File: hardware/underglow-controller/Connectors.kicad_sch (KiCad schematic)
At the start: 3 parts, among them J4 DTM1312PA12PBR008, J5 Conn_01x10

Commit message: i can't believe what they did to my boy
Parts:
- removed H1: MountingHole_Pad, MountingHole:MountingHole_3.2mm_M3_DIN965_Pad, symbol Mechanical:MountingHole_Pad
- added D5: D_Small, Diode_SMD:D_SOD-123F, symbol Device:D_Small
- added D7, D8: PESD2CANFD24V-T, Package_TO_SOT_SMD:SOT-23, symbol Device:D_TVS_Dual_AAC
- added F2: Fuse, ConeCodes:Keystone-3587-10TR, symbol Device:Fuse
- added J3: Conn_01x04, Connector_PinHeader_1.27mm:PinHeader_1x04_P1.27mm_Vertical, symbol Connector_Generic:Conn_01x04
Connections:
- net CAN_N: now also J4.B1, D8.2 (A2); no longer J4.B12
- net CAN_P: now also J4.B12, D8.1 (A1); no longer J4.B1
- net CONN_ESP_USB_D_N: now also J4.B4, D7.1 (A1); no longer J5.6 (Pin_6)
- net CONN_ESP_USB_D_P: now also J4.B5, D7.2 (A2); no longer J5.5 (Pin_5)
- net CONN_RP_USB_D_N: now also J3.3 (Pin_3); no longer J5.4 (Pin_4)
- net CONN_RP_USB_D_P: now also J3.2 (Pin_2); no longer J5.3 (Pin_3)
- net GND: now also D7.3 (common), D8.3 (common), J3.4 (Pin_4); no longer J4.A12
- net VBAT: now also D5.2 (A); no longer J4.A11
- net GPO4 renamed VOUT
- net GPO5: no longer names the net of J4.A6
- net GPO6: no longer names the net of J4.A5
- new net FUSE_IN: F2.2, J4.A12
- new net FUSE_OUT: F2.1
- new net VIN: D5.1 (K)
- no-connect marks 1 -> 2

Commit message: urmom
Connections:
- net VBAT is gone; now on net IGNITION: D5.2 (A)
- net CAN_N: now also J4.B12; no longer J4.B1
- net CAN_P: now also J4.B1; no longer J4.B12
- net GND: now also J4.A5
- net LEDA_OUT: now also J4.A4
- net VOUT: now also J4.A11; no longer J4.A4
- net IGNITION: now reaches J4.A6
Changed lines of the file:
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@@
+    (stroke (width 0) (type default) (color 0 0 0 0))
+  )
+  (wire (pts (xy 101.6 69.215) (xy 116.205 69.215))
     (stroke (width 0) (type default) (color 0 0 0 0))
   )
@@
     (stroke (width 0) (type default) (color 0 0 0 0))
   )
+  (wire (pts (xy 96.52 66.675) (xy 116.205 66.675))
+    (stroke (width 0) (type default) (color 0 0 0 0))
+  )
   (wire (pts (xy 57.785 84.455) (xy 70.485 84.455))
     (stroke (width 0) (type default) (color 0 0 0 0))
   )
-  (wire (pts (xy 101.6 64.135) (xy 116.205 64.135))
+  (wire (pts (xy 101.6 81.915) (xy 116.205 81.915))
     (stroke (width 0) (type default) (color 0 0 0 0))
   )
@@
     (stroke (width 0) (type default) (color 0 0 0 0))
   )
+  (wire (pts (xy 96.52 64.135) (xy 116.205 64.135))
+    (stroke (width 0) (type default) (color 0 0 0 0))
+  )
   (wire (pts (xy 96.52 79.375) (xy 116.205 79.375))
     (stroke (width 0) (type default) (color 0 0 0 0))
   )
   (wire (pts (xy 141.605 56.515) (xy 168.91 56.515))
-    (stroke (width 0) (type default) (color 0 0 0 0))
-  )
-  (wire (pts (xy 34.925 60.96) (xy 53.34 60.96))
-    (stroke (width 0) (type default) (color 0 0 0 0))
-  )
-  (wire (pts (xy 84.455 93.345) (xy 104.14 93.345))
     (stroke (width 0) (type default) (color 0 0 0 0))
   )
@@
     (effects (font (size 1.27 1.27)) (justify right bottom))
   )
-  (label "VBAT" (at 20.32 82.55 0)
+  (label "IGNITION" (at 20.32 82.55 0)
+    (effects (font (size 1.27 1.27)) (justify left bottom))
+  )
+  (label "LEDA" (at 101.6 64.135 0)
     (effects (font (size 1.27 1.27)) (justify left bottom))
   )
@@
     (effects (font (size 1.27 1.27)) (justify left bottom))
   )
-  (label "VOUT" (at 101.6 64.135 0)
-    (effects (font (size 1.27 1.27)) (justify left bottom))
-  )
-  (label "CAN_N" (at 161.29 56.515 180)
+  (label "VOUT" (at 101.6 81.915 0)
+    (effects (font (size 1.27 1.27)) (justify left bottom))
+  )
+  (label "CAN_N" (at 160.655 84.455 180)
     (effects (font (size 1.27 1.27)) (justify right bottom))
   )
@@
     (effects (font (size 1.27 1.27)) (justify left bottom))
   )
-  (label "VBAT" (at 45.085 76.2 0)
-    (effects (font (size 1.27 1.27)) (justify left bottom))
-  )
   (label "GPO1" (at 101.6 56.515 0)
     (effects (font (size 1.27 1.27)) (justify left bottom))
@@
     (effects (font (size 1.27 1.27)) (justify right bottom))
   )
+  (label "IGNITION" (at 101.6 69.215 0)
+    (effects (font (size 1.27 1.27)) (justify left bottom))
+  )
   (label "MOTOR2_OUT2" (at 100.965 79.375 0)
     (effects (font (size 1.27 1.27)) (justify left bottom))
@@
     (effects (font (size 1.27 1.27)) (justify left bottom))
   )
-  (label "CAN_P" (at 161.29 84.455 180)
+  (label "CAN_P" (at 160.655 56.515 180)
     (effects (font (size 1.27 1.27)) (justify right bottom))
   )
@@
     (effects (font (size 1.27 1.27)) (justify right bottom))
   )
-  (label "IGN_IN" (at 88.9 93.345 0)
-    (effects (font (size 1.27 1.27)) (justify left bottom))
-  )
   (label "CONN_RP_USB_D_P" (at 55.88 120.015 0)
     (effects (font (size 1.27 1.27)) (justify left bottom))
@@
     (effects (font (size 1.27 1.27)) (justify left))
   )
-  (hierarchical_label "LEDA_OUT" (shape input) (at 179.705 73.025 0)
-    (effects (font (size 1.27 1.27)) (justify left))
+  (hierarchical_label "LEDA_OUT" (shape input) (at 96.52 64.135 180)
+    (effects (font (size 1.27 1.27)) (justify right))
   )
   (hierarchical_label "CONN_RP_USB_D_N" (shape bidirectional) (at 51.435 122.555 180)
@@
     (effects (font (size 1.27 1.27)) (justify right))
   )
+  (hierarchical_label "VOUT" (shape input) (at 101.6 81.915 180)
+    (effects (font (size 1.27 1.27)) (justify right))
+  )
   (hierarchical_label "GPO2" (shape input) (at 96.52 59.055 180)
     (effects (font (size 1.27 1.27)) (justify right))
   )
-  (hierarchical_label "CAN_P" (shape bidirectional) (at 168.91 84.455 0)
-    (effects (font (size 1.27 1.27)) (justify left))
-  )
-  (hierarchical_label "CAN_N" (shape bidirectional) (at 168.91 56.515 0)
+  (hierarchical_label "CAN_P" (shape bidirectional) (at 168.91 56.515 0)
+    (effects (font (size 1.27 1.27)) (justify left))
+  )
+  (hierarchical_label "CAN_N" (shape bidirectional) (at 168.91 84.455 0)
     (effects (font (size 1.27 1.27)) (justify left))
   )
@@
     )
     (property "Datasheet" "" (id 3) (at 187.325 148.59 0)
-      (effects (font (size 1.27 1.27)) hide)
-    )
-    (pin "1")
-  )
-  (symbol (lib_id "power:GND") (at 34.925 60.96 270) (unit 1)
-    (in_bom yes) (on_board yes) (fields_autoplaced)
-    (property "Reference" "#PWR0101" (id 0) (at 28.575 60.96 0)
-      (effects (font (size 1.27 1.27)) hide)
-    )
-    (property "Value" "GND" (id 1) (at 31.115 60.9599 90)
-      (effects (font (size 1.27 1.27)) (justify right))
-    )
-    (property "Footprint" "" (id 2) (at 34.925 60.96 0)
-      (effects (font (size 1.27 1.27)) hide)
-    )
-    (property "Datasheet" "" (id 3) (at 34.925 60.96 0)
       (effects (font (size 1.27 1.27)) hide)
     )
@@
       (effects (font (size 1.27 1.27)) hide)
     )
+    (pin "1")
+  )
+  (symbol (lib_id "power:GND") (at 96.52 66.675 270) (unit 1)
+    (in_bom yes) (on_board yes) (fields_autoplaced)
+    (property "Reference" "#PWR0101" (id 0) (at 90.17 66.675 0)
+      (effects (font (size 1.27 1.27)) hide)
+    )
+    (property "Value" "GND" (id 1) (at 92.71 66.6749 90)
+      (effects (font (size 1.27 1.27)) (justify right))
+    )
+    (property "Footprint" "" (id 2) (at 96.52 66.675 0)
+      (effects (font (size 1.27 1.27)) hide)
+    )
+    (property "Datasheet" "" (id 3) (at 96.52 66.675 0)
+      (effects (font (size 1.27 1.27)) hide)
+    )

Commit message: updates nearly complete
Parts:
- removed J5: Conn_01x10, Connector_PinHeader_2.54mm:PinHeader_1x10_P2.54mm_Vertical, symbol Connector_Generic:Conn_01x10
- added C6: 10uF, Capacitor_SMD:C_0805_2012Metric, symbol Device:C_Small
- added J5: Conn_01x05, Connector_PinHeader_1.27mm:PinHeader_1x05_P1.27mm_Vertical, symbol Connector_Generic:Conn_01x05
- F2: MPN (none) -> 3587-10TR
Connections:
- net +3V3: now also C6.2, J5.1 (Pin_1)
- net GND: now also C6.1, J5.2 (Pin_2)
- net MISO: now also J5.4 (Pin_4)
- net MOSI: now also J5.5 (Pin_5)
- net SCLK: now also J5.3 (Pin_3)
- no-connect marks 2 -> 1

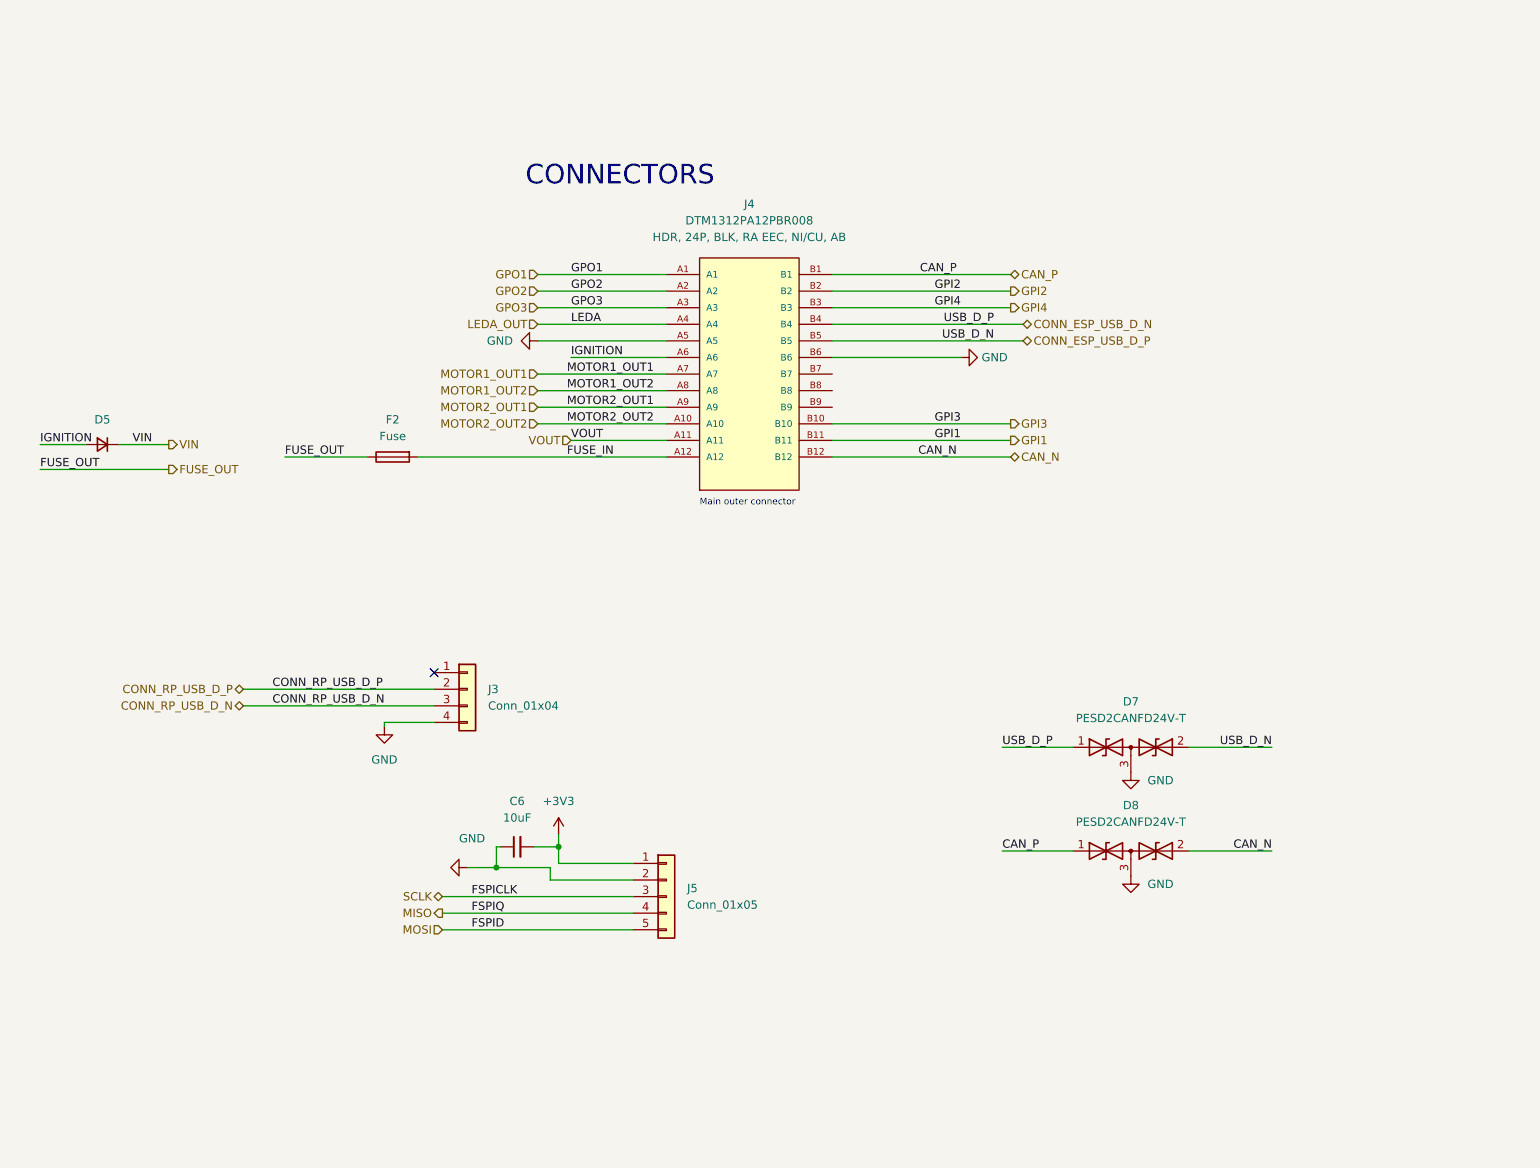
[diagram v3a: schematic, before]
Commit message: add USB VIN
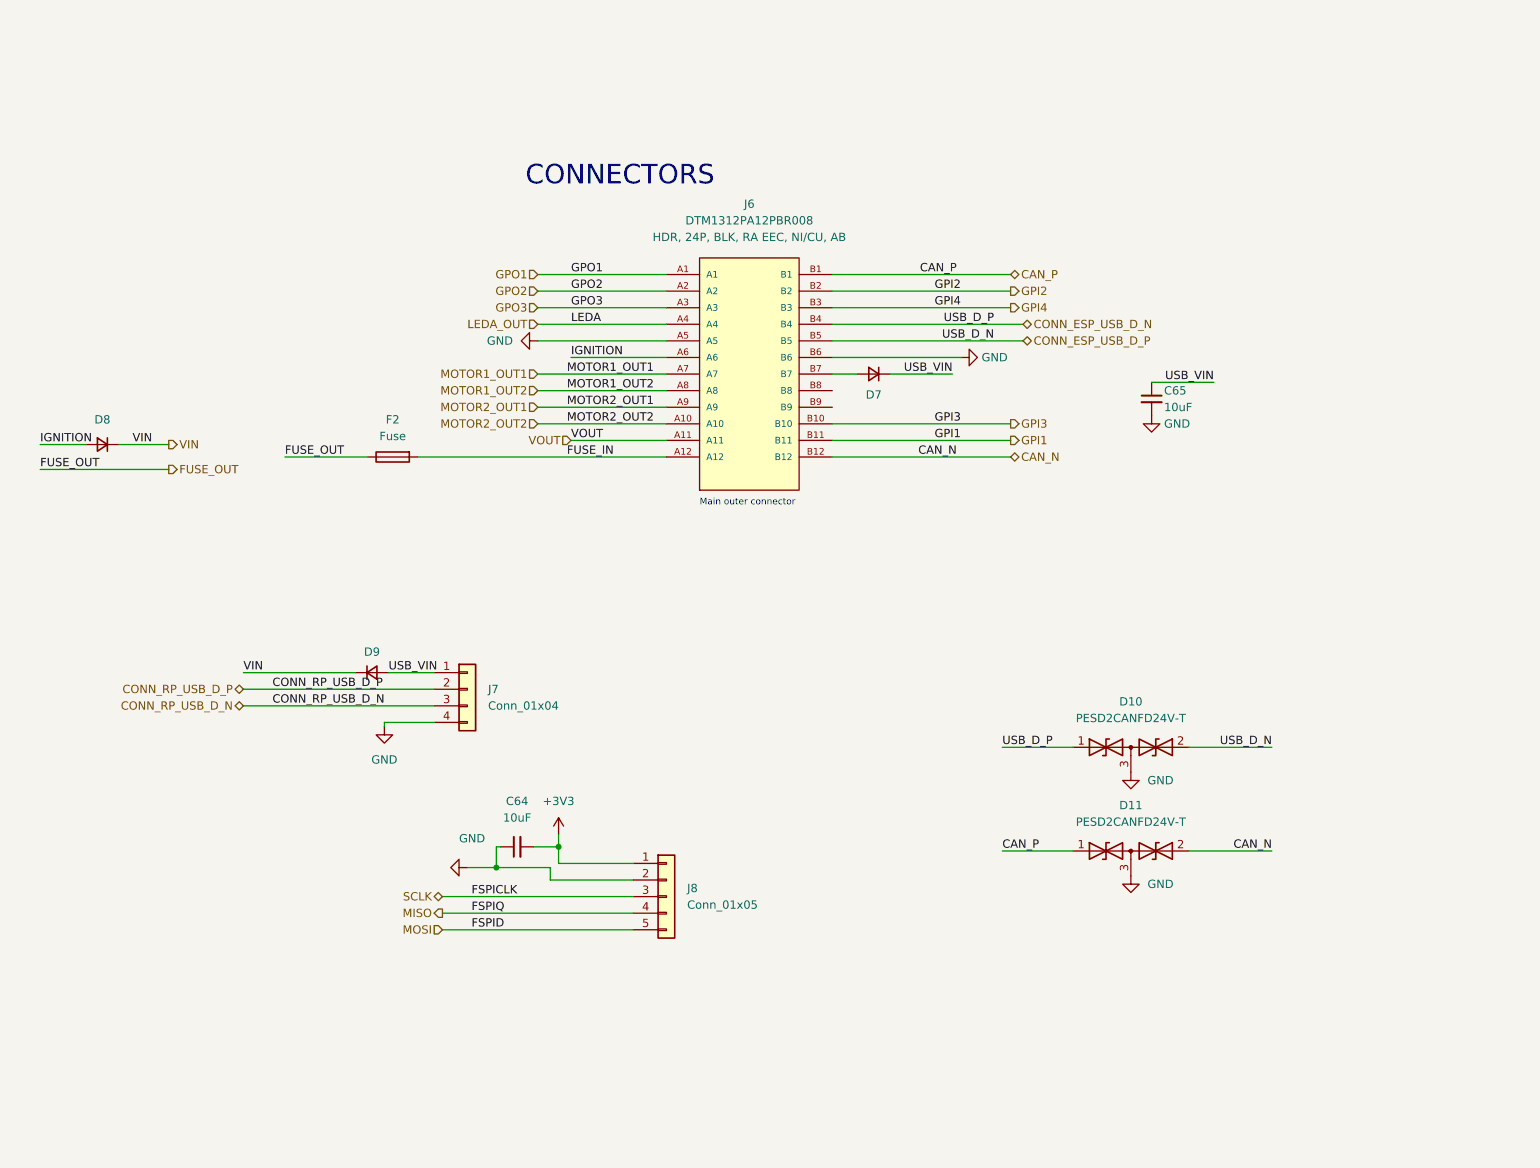
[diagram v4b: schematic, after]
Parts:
- added C65: 10uF, Capacitor_SMD:C_0805_2012Metric, symbol Device:C_Small
- added D7, D9: D_Small, Diode_SMD:D_SOD-123F, symbol Device:D_Small
- renumbered C6 to C64, D7 to D10, D8 to D11, D5 to D8, J4 to J6, J3 to J7, J5 to J8
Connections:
- net GND: now also C65.2
- net VIN: now also D9.1 (K)
- net at J6.B7: now also D7.2 (A)
- net USB_VIN: now reaches J7.1 (Pin_1)
- net USB_VIN: now also C65.1, D7.1 (K), D9.2 (A)
- no-connect marks 1 -> 0
